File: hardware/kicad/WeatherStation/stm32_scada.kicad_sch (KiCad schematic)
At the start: 20 parts, among them J16 RS485 Bus (Phoenix MC), J17 ESP32-S3 Bridge (Header), SW3 MODE_SELECT, U10 STM32F407VGT6, U11 MAX3485ESA+, Y1 8MHz

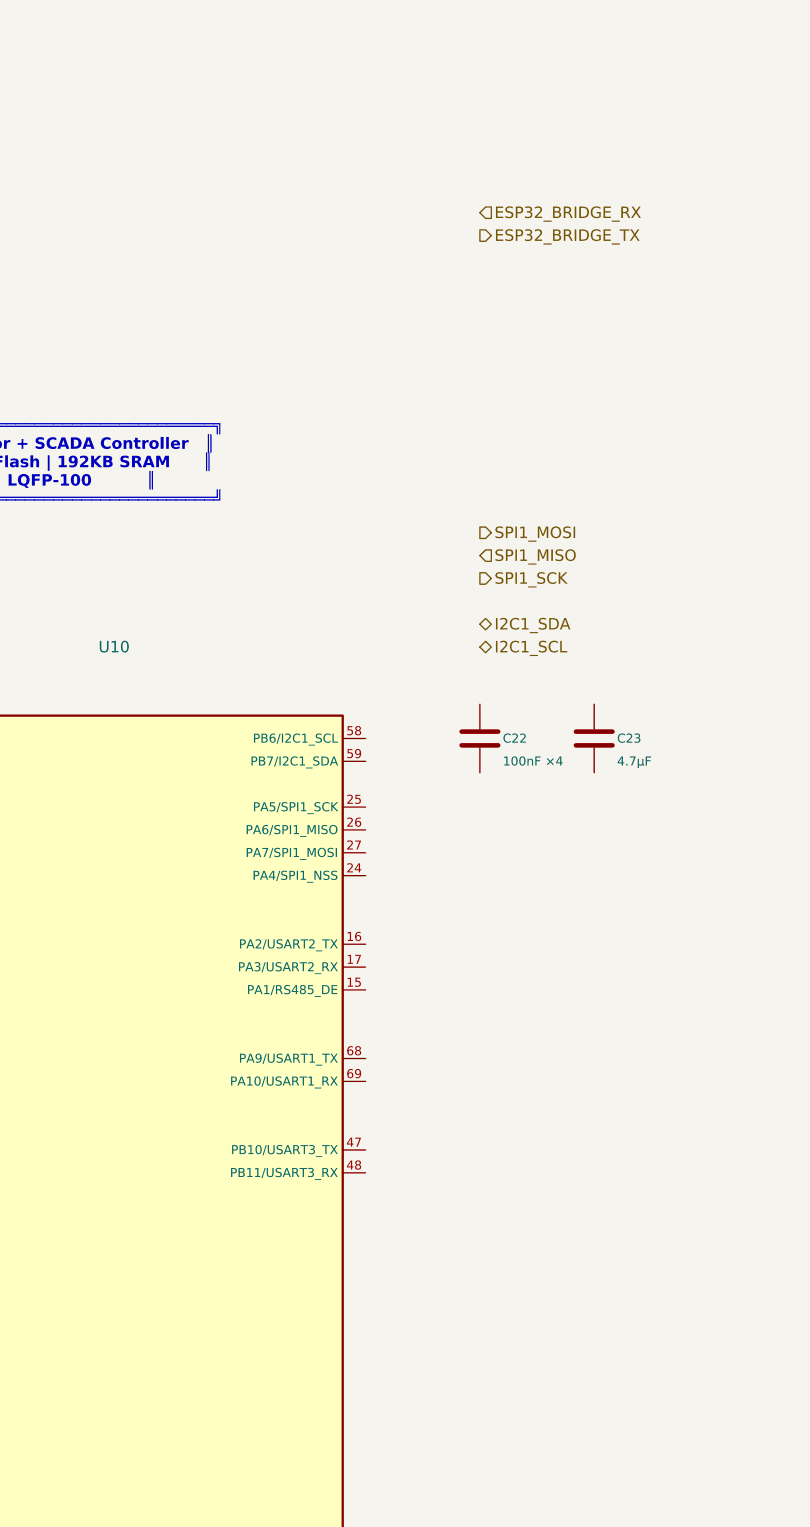
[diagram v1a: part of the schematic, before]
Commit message: fix: remove invalid ;; comments from KiCad schematics and add SD card circuit
KiCad's S-expression parser does not support semicolon comments.
All ;; comment lines have been stripped from the 5 .kicad_sch files
and WeatherStation.kicad_sym to fix "Expecting '('" parse errors.

Also adds the SD card circuit to communication.kicad_sch:
- J22 MicroSD_SPI holder with SPI2 bus connections
- C38 100nF VCC decoupling capacitor
- R27 10k pull-up on card detect line
- SPI2_SCK/MISO/MOSI/SD_CS/SD_DET hierarchical labels
- Wire routing and power symbols (+3V3, GND)

https://claude.ai/code/session_01XHnfZQ5BbxTCTBMCteQyVe
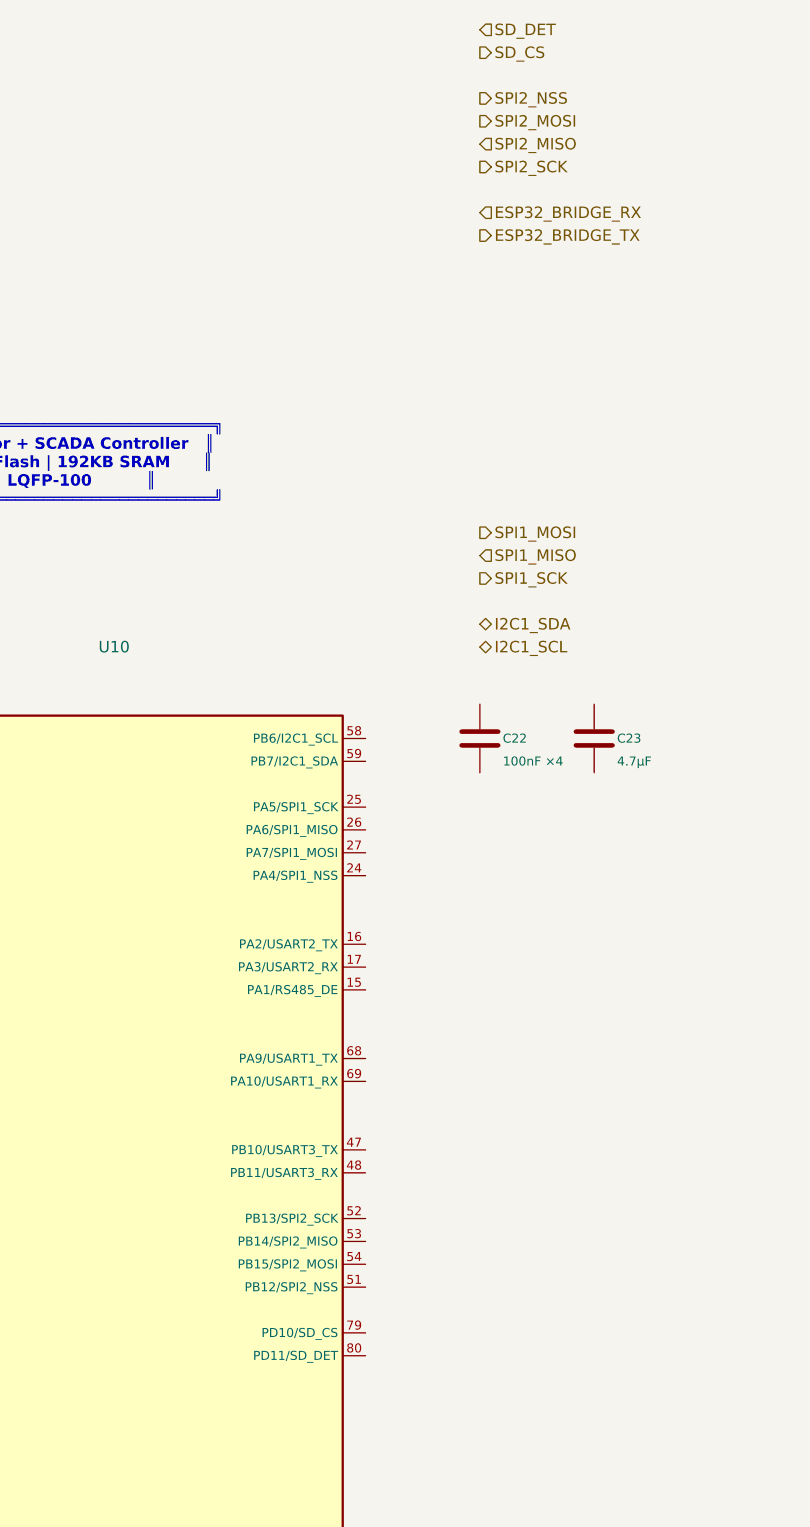
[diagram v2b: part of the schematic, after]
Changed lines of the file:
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@@
     (comment 3 "Industrial grade: -40C to +105C, IP65 enclosure, TVS protection")
   )
-  ;; =====================================================================
-  ;; STM32F407VGT6 — Main MCU (Industrial -40C to +105C)
-  ;; =====================================================================
   (text "╔══════════════════════════════════════════════════════════╗\n║   STM32F407VGT6 — Industrial Sensor + SCADA Controller   ║\n║   ARM Cortex-M4F @ 168 MHz | 1MB Flash | 192KB SRAM      ║\n║   Temp: -40°C to +105°C (Industrial) | LQFP-100          ║\n╚══════════════════════════════════════════════════════════╝"
     (at 76.2 25.4 0) (effects (font (size 1.27 1.27) (bold yes)) (justify left))
   )
-  ;; U10 — STM32F407VGT6
   (symbol (lib_id "MCU_ST:STM32F407VGT6") (at 127 101.6 0) (unit 1)
     (in_bom yes) (on_board yes) (dnp no)
@@
     (property "Value" "STM32F407VGT6" (at 127 152.4 0) (effects (font (size 1.27 1.27))))
   )
-  ;; Y1 — 8 MHz HSE Crystal
   (symbol (lib_id "Device:Crystal") (at 76.2 132.08 0) (unit 1)
     (in_bom yes) (on_board yes) (dnp no)
@@
     (property "Value" "8MHz" (at 76.2 137.16 0) (effects (font (size 1.27 1.27))))
   )
-  ;; Crystal load caps (2× 20pF)
   (symbol (lib_id "Device:C") (at 68.58 139.7 0) (unit 1)
     (in_bom yes) (on_board yes) (dnp no)
@@
     (property "Value" "20pF" (at 86.36 142.24 0) (effects (font (size 1.0 1.0)) (justify left)))
   )
-  ;; MCU decoupling caps (4× 100nF + 1× 4.7µF bulk)
   (symbol (lib_id "Device:C") (at 167.64 55.88 0) (unit 1)
     (in_bom yes) (on_board yes) (dnp no)
@@
     (property "Value" "4.7µF" (at 182.88 58.42 0) (effects (font (size 1.0 1.0)) (justify left)))
   )
-  ;; NRST pull-up + filter cap
   (symbol (lib_id "Device:R") (at 83.82 78.74 0) (unit 1)
     (in_bom yes) (on_board yes) (dnp no)
@@
     (property "Value" "100nF" (at 86.36 91.44 0) (effects (font (size 1.0 1.0)) (justify left)))
   )
-  ;; BOOT0 pull-down (normal boot from flash)
   (symbol (lib_id "Device:R") (at 83.82 96.52 0) (unit 1)
     (in_bom yes) (on_board yes) (dnp no)
@@
     (property "Value" "10k" (at 86.36 99.06 0) (effects (font (size 1.0 1.0)) (justify left)))
   )
-  ;; =====================================================================
-  ;; RS485 TRANSCEIVER — MAX3485ESA+ (Industrial -40C to +85C)
-  ;; =====================================================================
   (text "╔══════════════════════════════════════════╗\n║   RS485 Modbus RTU Interface             ║\n║   MAX3485ESA+ half-duplex transceiver    ║\n║   120Ω termination + TVS protection      ║\n╚══════════════════════════════════════════╝"
     (at 220 25.4 0) (effects (font (size 1.27 1.27) (bold yes)) (justify left))
   )
-  ;; U11 — MAX3485ESA+ RS485 Transceiver
   (symbol (lib_id "Interface_UART:MAX3485") (at 243.84 71.12 0) (unit 1)
     (in_bom yes) (on_board yes) (dnp no)
@@
     (property "Value" "MAX3485ESA+" (at 243.84 83.82 0) (effects (font (size 1.27 1.27))))
   )
-  ;; RS485 bus termination resistor (120Ω at end of bus)
   (symbol (lib_id "Device:R") (at 271.78 71.12 90) (unit 1)
     (in_bom yes) (on_board yes) (dnp no)
@@
     (property "Value" "120Ω" (at 271.78 76.2 0) (effects (font (size 1.0 1.0))))
   )
-  ;; TVS diode on RS485 A/B lines
   (symbol (lib_id "Device:D_TVS") (at 264.16 83.82 90) (unit 1)
     (in_bom yes) (on_board yes) (dnp no)
@@
     (property "Value" "SMBJ6.0CA" (at 274.32 83.82 0) (effects (font (size 1.0 1.0))))
   )
-  ;; VCC decoupling for MAX3485
   (symbol (lib_id "Device:C") (at 256.54 60.96 0) (unit 1)
     (in_bom yes) (on_board yes) (dnp no)
@@
     (property "Value" "100nF" (at 259.08 63.5 0) (effects (font (size 1.0 1.0)) (justify left)))
   )
-  ;; J16 — RS485 Bus Connector (A, B, GND, Shield)
   (symbol (lib_id "Connector:Conn_01x04") (at 299.72 71.12 0) (unit 1)
     (in_bom yes) (on_board yes) (dnp no)
@@
     (property "Value" "RS485 Bus (Phoenix MC)" (at 314.96 60.96 0) (effects (font (size 1.0 1.0)) (justify left)))
   )
-  ;; =====================================================================
-  ;; ESP32-S3 BRIDGE — USART3 interconnect
-  ;; =====================================================================
   (text "╔══════════════════════════════════════════╗\n║   ESP32-S3 Bridge (Cloud Connectivity)   ║\n║   USART3 @ 921600 baud, 3.3V levels     ║\n║   Framed protocol with CRC16            ║\n╚══════════════════════════════════════════╝"
     (at 220 115 0) (effects (font (size 1.27 1.27) (bold yes)) (justify left))
   )
-  ;; J17 — ESP32-S3 Bridge Header (TX, RX, 3V3, GND)
   (symbol (lib_id "Connector:Conn_01x04") (at 269.24 139.7 0) (unit 1)
     (in_bom yes) (on_board yes) (dnp no)
@@
     (property "Value" "ESP32-S3 Bridge (Header)" (at 289.56 129.54 0) (effects (font (size 1.0 1.0)) (justify left)))
   )
-  ;; Series resistors for bridge UART (100Ω protection)
   (symbol (lib_id "Device:R") (at 243.84 134.62 90) (unit 1)
     (in_bom yes) (on_board yes) (dnp no)
@@
     (property "Value" "100Ω" (at 243.84 152.4 0) (effects (font (size 1.0 1.0))))
   )
-  ;; =====================================================================
-  ;; MODE SELECT DIP SWITCH
-  ;; =====================================================================
   (text "╔════════════════════════════════════╗\n║   Mode Select DIP Switch           ║\n║   SW1=0,SW2=0: Cloud               ║\n║   SW1=1,SW2=0: SCADA               ║\n║   SW1=0,SW2=1: Hybrid              ║\n║   SW1=1,SW2=1: Hybrid (reserved)   ║\n╚════════════════════════════════════╝"
     (at 55.88 165.1 0) (effects (font (size 1.27 1.27) (bold yes)) (justify left))
   )
-  ;; SW3 — Mode DIP Switch (2-position)
   (symbol (lib_id "Switch:SW_DIP_x02") (at 76.2 187.96 0) (unit 1)
     (in_bom yes) (on_board yes) (dnp no)
@@
     (property "Value" "MODE_SELECT" (at 76.2 195.58 0) (effects (font (size 1.27 1.27))))
   )
-  ;; Pull-down resistors for DIP switch
   (symbol (lib_id "Device:R") (at 60.96 193.04 0) (unit 1)
     (in_bom yes) (on_board yes) (dnp no)
@@
     (property "Value" "10k" (at 53.34 195.58 0) (effects (font (size 1.0 1.0)) (justify right)))
   )
-  ;; =====================================================================
-  ;; STATUS LEDs (3× for Mode indication)
-  ;; =====================================================================
   (text "LEDs:\n  PD0 = Green (Status/Heartbeat)\n  PD1 = Red (Error/Fault)\n  PD2 = Amber (SCADA Active)"
     (at 55.88 215 0) (effects (font (size 1.0 1.0)) (justify left))
   )
-  ;; =====================================================================
-  ;; Important Design Notes
-  ;; =====================================================================
   (text "DESIGN NOTES:\n\n1. STM32F407VGT6 handles ALL sensor acquisition and local processing\n2. ESP32-S3 handles cloud connectivity ONLY (WiFi, BLE, MQTT, HTTP)\n3. STM32 sends processed readings to ESP32 via USART3 bridge\n4. RS485 Modbus runs on STM32 USART2 via MAX3485 transceiver\n5. Both MCUs share 3.3V power rail from TPS63020\n6. IWDG on STM32 provides 4-second watchdog protection\n7. DIP switch on PE0/PE1 selects operating mode at boot\n8. All external I/O protected with TVS diodes\n\nRS485 BUS WIRING:\n  - Use twisted pair cable (Cat5e or dedicated RS485 cable)\n  - 120Ω termination at each end of bus\n  - Maximum bus length: 1200m at 9600 baud\n  - Maximum 32 devices on bus\n  - Shield connected to GND at one end only\n\nJ16 PINOUT (Phoenix Contact MC series):\n  Pin 1 = A (non-inverting, D+)\n  Pin 2 = B (inverting, D-)\n  Pin 3 = GND (signal ground)\n  Pin 4 = Shield (chassis ground)"
     (at 55.88 240 0) (effects (font (size 1.0 1.0)) (justify left))
   )
-  ;; =====================================================================
-  ;; Hierarchical Labels
-  ;; =====================================================================
   (hierarchical_label "I2C1_SCL" (shape bidirectional) (at 167.64 45.72 0) (effects (font (size 1.27 1.27)) (justify left))
   )
@@
   (hierarchical_label "SPI1_MOSI" (shape output) (at 167.64 33.02 0) (effects (font (size 1.27 1.27)) (justify left))
   )
+  (hierarchical_label "SPI2_SCK" (shape output) (at 167.64 -7.62 0) (effects (font (size 1.27 1.27)) (justify left))
+  )
+  (hierarchical_label "SPI2_MISO" (shape input) (at 167.64 -10.16 0) (effects (font (size 1.27 1.27)) (justify left))
+  )
+  (hierarchical_label "SPI2_MOSI" (shape output) (at 167.64 -12.7 0) (effects (font (size 1.27 1.27)) (justify left))
+  )
+  (hierarchical_label "SPI2_NSS" (shape output) (at 167.64 -15.24 0) (effects (font (size 1.27 1.27)) (justify left))
+  )
+  (hierarchical_label "SD_CS" (shape output) (at 167.64 -20.32 0) (effects (font (size 1.27 1.27)) (justify left))
+  )
+  (hierarchical_label "SD_DET" (shape input) (at 167.64 -22.86 0) (effects (font (size 1.27 1.27)) (justify left))
+  )
   (hierarchical_label "RS485_A" (shape bidirectional) (at 309.88 67.31 0) (effects (font (size 1.27 1.27)) (justify left))
